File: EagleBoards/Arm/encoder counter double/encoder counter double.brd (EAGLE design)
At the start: 160 x 100 mm, 15 parts, among them X2 22-23-2021_100MILHEADER, X3 22-23-2041, X4 22-23-2021_100MILHEADER, X5 22-23-2021_100MILHEADER, X6 22-23-2021_100MILHEADER

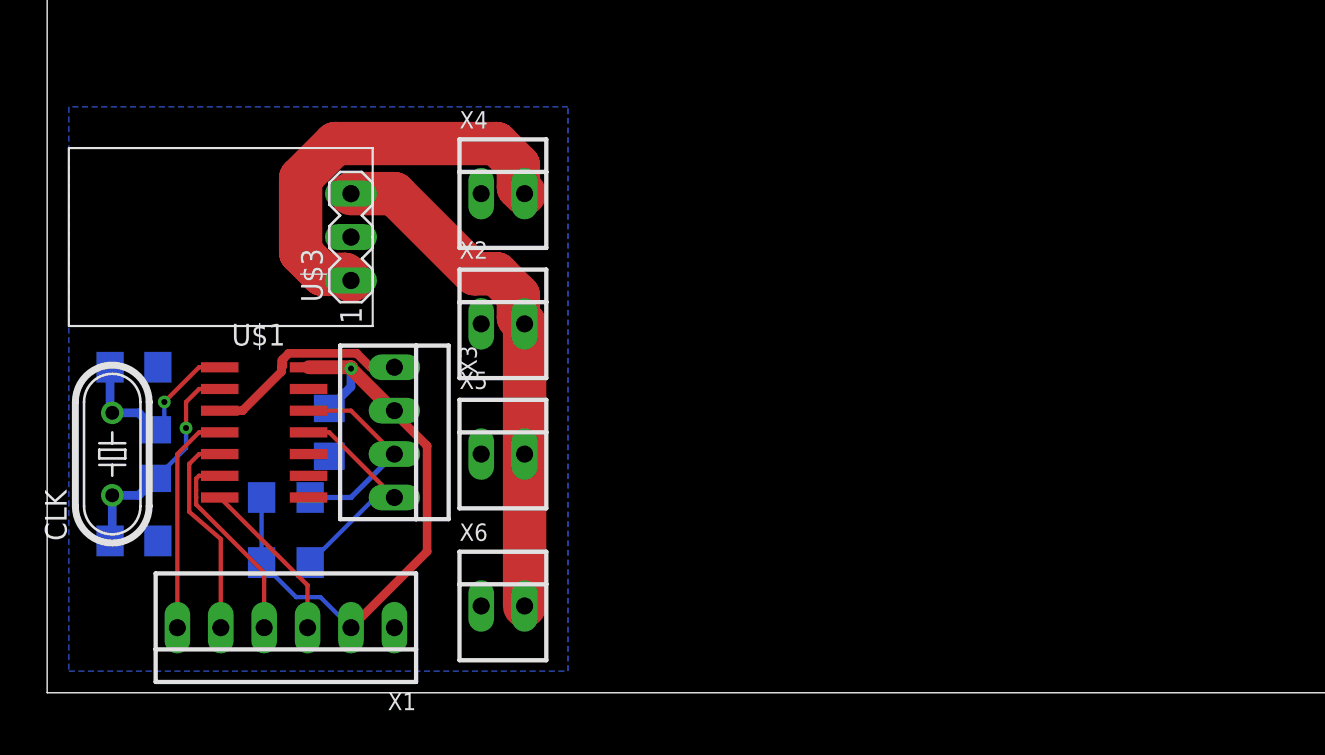
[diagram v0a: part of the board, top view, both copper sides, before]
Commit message: pre silk encoder brds. layout ready for review
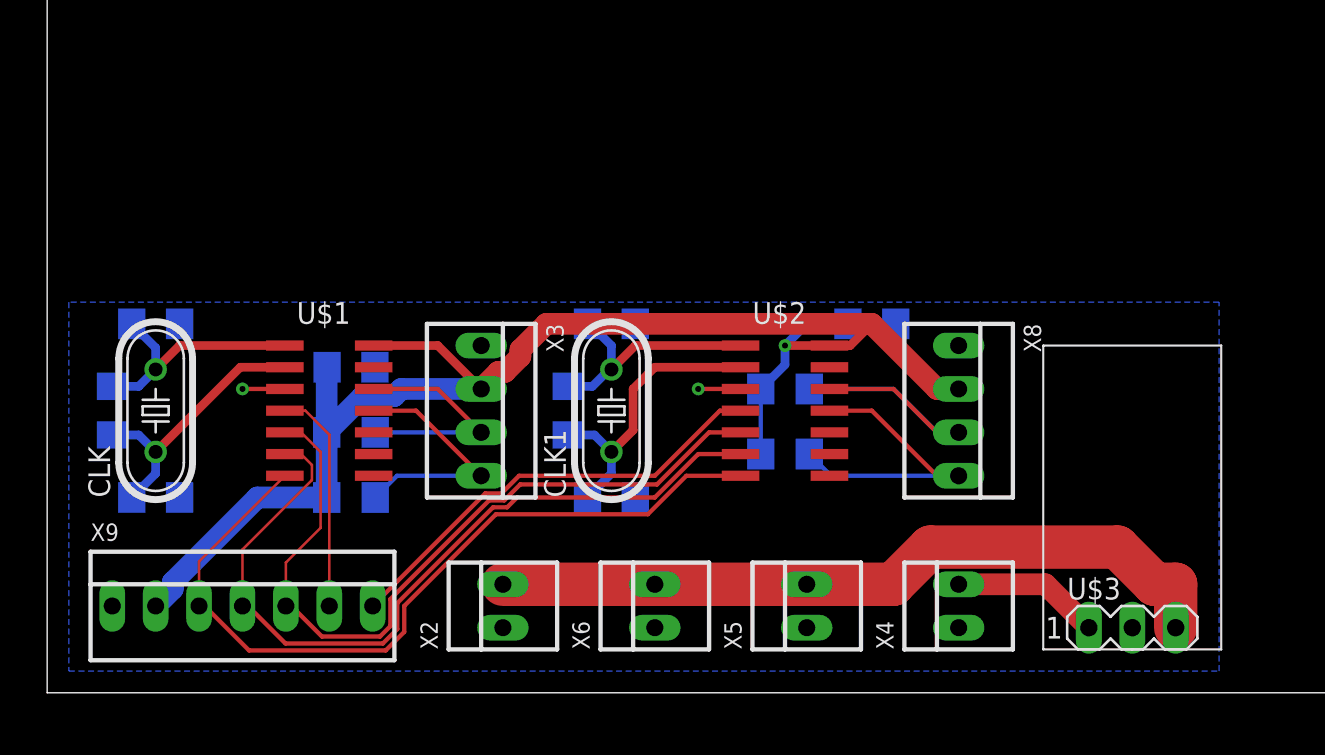
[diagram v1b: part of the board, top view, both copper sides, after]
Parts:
- removed X1: (no value), HuskyRobotics17-18:22-23-2061
- added C4: 18p, rcl:C1206
- added C5, C6: .1u, rcl:C1206
- added CLK1: HC-49CRYSTAL, HuskyRobotics17-18:HC49/S
- added R4, R5: 10k, rcl:R1206
- added R6: 1M, rcl:R1206
- added U$2: LS7366R, HuskyRobotics17-18:SO14
- added X8: 22-23-2041, HuskyRobotics17-18:22-23-2041
- added X9: 22-23-2071, con-molex:22-23-2071
- moved U$3 51.1 mm to (63.5, 3.81), turned to 0 degrees
- moved X4 36.0 mm to (53.3, 5.08), turned to 90 degrees
- moved X5 19.9 mm to (44.5, 5.08), turned to 90 degrees
- moved C3 17.7 mm to (33.0, 21.6), turned to 0 degrees
- moved X2 16.5 mm to (26.7, 5.08), turned to 90 degrees
- moved X6 8.89 mm to (35.6, 5.08), turned to 90 degrees
- moved R1 5.39 mm to (17.8, 15.2)
- moved R2 5.39 mm to (17.8, 11.4)
- moved X3 5.24 mm to (25.4, 16.5)
- moved U$1 4.02 mm to (16.5, 16.5)
- moved CLK 3.59 mm to (6.35, 16.5)
- moved R3 3.59 mm to (3.81, 16.5)
- moved C1 2.84 mm to (6.35, 21.6)
- moved C2 2.84 mm to (6.35, 11.4)
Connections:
- new net A1: R4.1, U$2.12, X8.3
- new net B1: R5.1, U$2.11, X8.4
- new net FCKI1: C4.2, CLK1.1, R6.1, U$2.2
- new net FCKO1: C3.2, CLK1.2, R6.2, U$2.1
- new net SS1: U$2.4, X9.7
- net GND: now also C3.1, C4.1, C5.2, C6.2, U$2.3, X8.1, X9.1; no longer C3.2, X1.1
- net MISO: now also U$2.6, X9.4; no longer X1.4
- net MOSI: now also U$2.7, X9.3; no longer X1.3
- net SCK: now also U$2.5, X9.5; no longer X1.5
- net SS: now also X9.6; no longer X1.6
- net VCC3: now also C5.1, C6.1, R4.2, R5.2, U$2.14, X8.2, X9.2; no longer C3.1, X1.2
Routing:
- net VCC3: track 35.0 -> 86.0 mm
- net MOSI: track 9.75 -> 47.6 mm
- net MISO: track 11.8 -> 47.3 mm
- net SCK: track 12.5 -> 45.6 mm
- net SS1: track 0.00 -> 26.3 mm
- net A1: track 0.00 -> 18.4 mm
- net B1: track 0.00 -> 18.4 mm
- net FCKI1: track 0.00 -> 17.2 mm
- net VIN: track 23.9 -> 8.67 mm
- net FCKO1: track 0.00 -> 14.5 mm
- net VCC5: track 30.6 -> 43.7 mm
- net GND: track 12.7 -> 4.96 mm, vias 0 -> 2
- net FCKO: track 11.6 -> 14.3 mm, vias 1 -> 0
- net FCKI: track 13.2 -> 15.8 mm, vias 1 -> 0
- net B: track 13.1 -> 14.6 mm
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
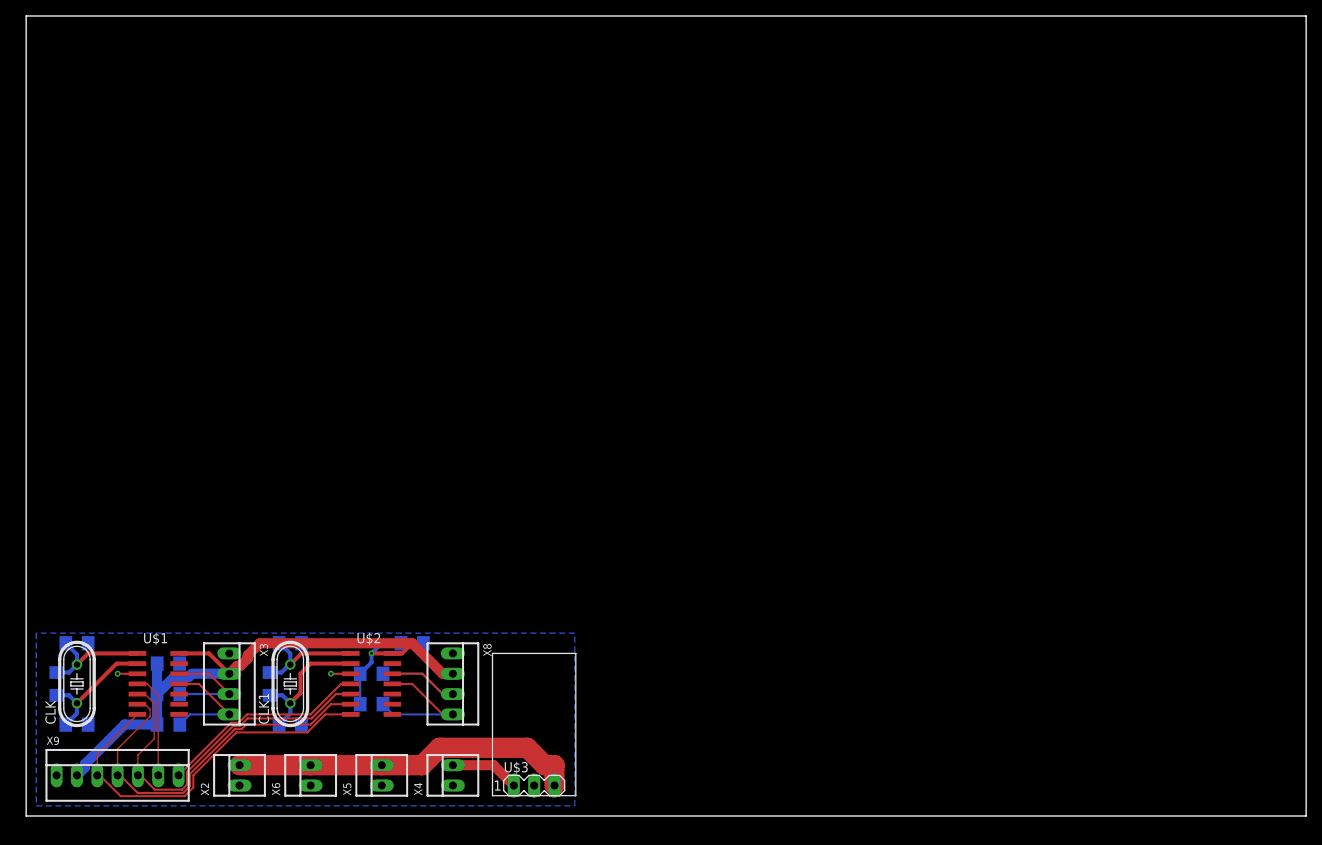
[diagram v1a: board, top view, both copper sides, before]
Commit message: encoder boards done
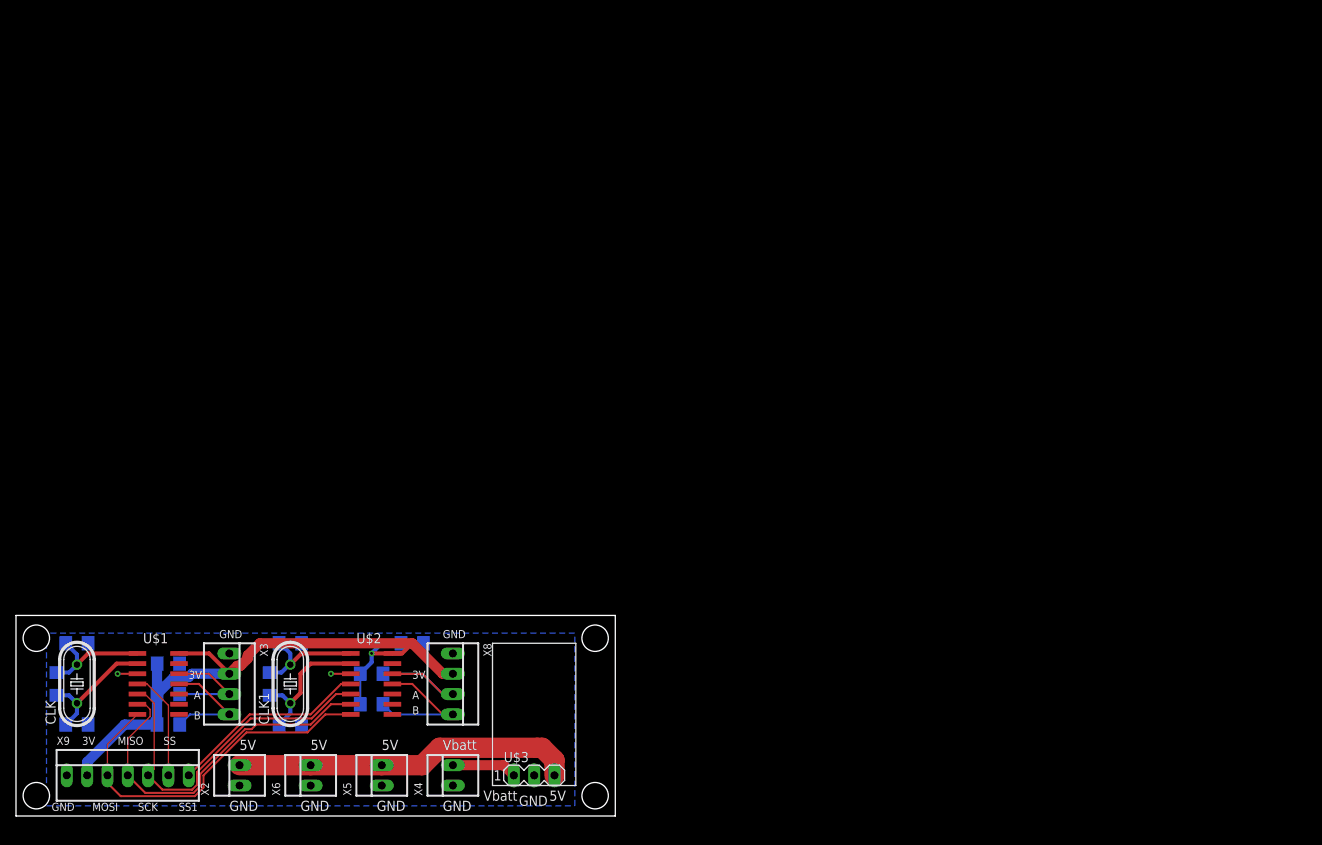
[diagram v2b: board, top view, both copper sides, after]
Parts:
- moved U$3 1.27 mm to (63.5, 5.08)
- moved X9 1.27 mm to (12.7, 5.08)
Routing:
- net SCK: track 45.6 -> 43.9 mm
- net MISO: track 47.3 -> 45.5 mm
- net SS1: track 26.3 -> 25.0 mm
- net MOSI: track 47.6 -> 46.3 mm
- net VCC5: track 43.7 -> 42.8 mm
- net VIN: track 8.67 -> 8.15 mm
- net SS: track 13.2 -> 13.7 mm
- net VCC3: track 86.0 -> 85.5 mm
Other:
- board size 160 x 100 mm -> 74.9 x 25.1 mm
- board text added: "3V"
- board text added: "5V"
- board text added: "A"
- board text added: "B"
- board text added: "GND"
- board text added: "MISO"
- board text added: "MOSI"
- board text added: "SCK"
- board text added: "SS"
- board text added: "SS1"
- board text added: "Vbatt"

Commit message: printed designs with gerbers
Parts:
- moved C6 1.27 mm to (49.5, 21.6)
- moved R4 1.27 mm to (44.5, 17.8)
- moved R5 1.27 mm to (44.5, 14.0)
- moved U$2 1.27 mm to (44.5, 16.5)
- moved X3 1.27 mm to (26.7, 16.5)
- moved X9 1.27 mm to (14.0, 5.08)
- moved C1 1.27 mm to (7.62, 21.6)
- moved C2 1.27 mm to (7.62, 11.4)
- moved CLK 1.27 mm to (7.62, 16.5)
- moved R3 1.27 mm to (5.08, 16.5)
- moved C5 1.27 mm to (19.1, 19.1)
- moved R1 1.27 mm to (19.1, 15.2)
- moved R2 1.27 mm to (19.1, 11.4)
- moved R6 1.27 mm to (31.8, 16.5)
- moved U$1 1.27 mm to (17.8, 16.5)
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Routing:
- net VIN: track 8.15 -> 16.3 mm
- net VCC5: track 42.8 -> 36.6 mm
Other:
- outline, holes or cut-outs redrawn
- board text added: "Dual Quadrature Decoder"
- board text added: "Husky Robotics 2018"
